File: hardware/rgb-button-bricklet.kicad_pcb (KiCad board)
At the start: 2 copper layers, 25 x 25 mm, 23 parts, among them P1 CON-SENSOR, P2 Boot, SW1 RGB_SWITCH_AD, U1 XMC1XXX24, U2 DRILL, U3 DRILL, U4 DRILL, U5 DRILL

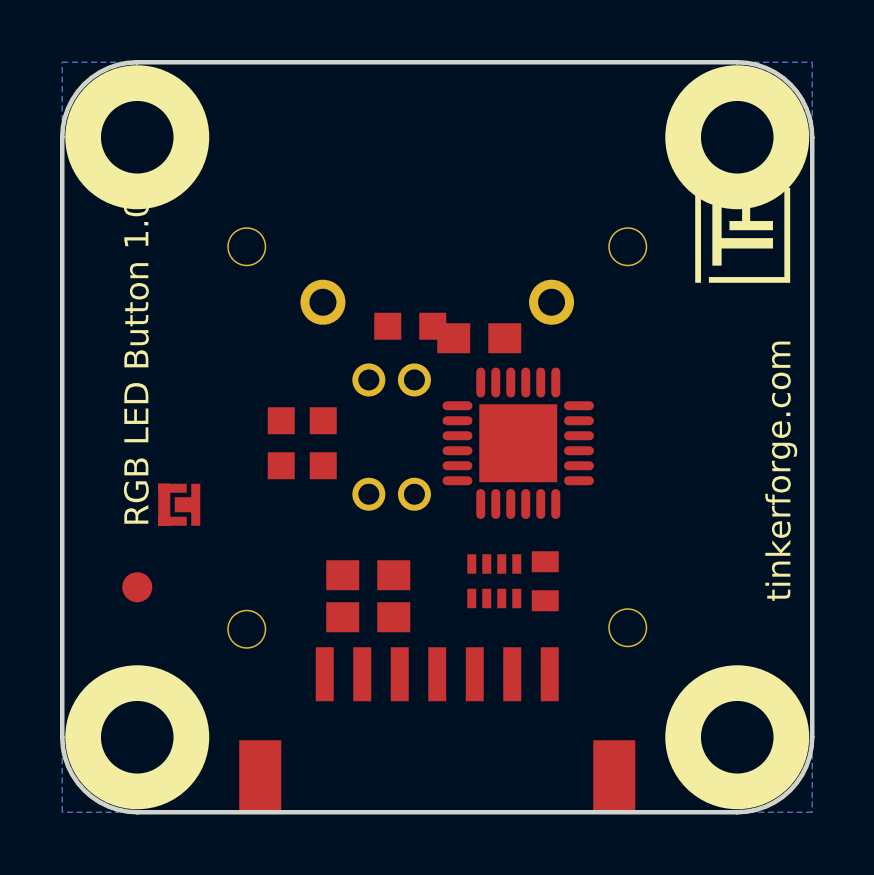
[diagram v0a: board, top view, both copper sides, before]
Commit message: change bricklet to 25x25mm size
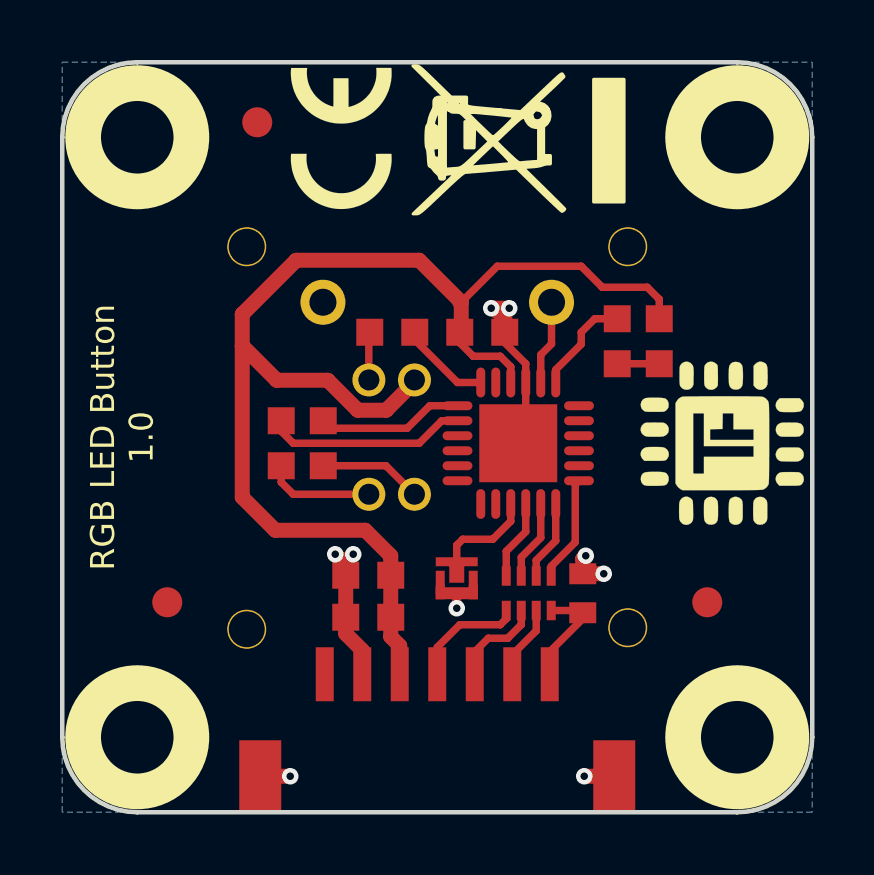
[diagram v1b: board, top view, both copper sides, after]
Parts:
- added D1: blue, kicad-libraries:D0603F, F.Cu at (159.1, 99.2)
- added R4: DNP, R0603F, F.Cu at (146.5, 102.6)
- C1: value 1uF -> TBD; footprint kicad-libraries:C0603E -> C0402E
- C2: value 10uF -> 1uF; footprint kicad-libraries:C0603E -> kicad-libraries:C0603F
- C3: value 100nF -> 10uF; footprint kicad-libraries:C0603E -> kicad-libraries:C0603F
- C4: value TBD -> 100nF; footprint kicad-libraries:C0402E -> kicad-libraries:C0603F
- G*** (x2), VAL: moved to F.Cu
- G***: moved to B.Cu
- R1: value DNP -> 1k
- R2, R3: footprint kicad-libraries:R0603F -> R0603F
- RP1: footprint kicad-libraries:4X0402 -> 4X0402
- SW1: footprint kicad-libraries:RGB_SWITCH_AD -> RGB_SWITCH_AD
- moved Fiducial_Mark 15.5 mm to (160.7, 107.9)
- moved G*** 10.5 mm to (161.2, 102.6), turned to 90 degrees
- moved P2 9.57 mm to (152.3, 107.1), turned to 90 degrees
- moved C1 7.19 mm to (156.6, 107.6), turned to 90 degrees
- moved R1 6.92 mm to (157.7, 99.2), turned to 270 degrees
- moved C4 6.02 mm to (149.4, 108.4), turned to 0 degrees
- moved R2 5.23 mm to (150.2, 98.9), turned to 180 degrees
- moved Fiducial_Mark 4.03 mm to (145.7, 91.9)
- moved G*** 3.78 mm to (159.0, 100.8), turned to 270 degrees
- moved VAL 2.60 mm to (148.5, 92.4), turned to 90 degrees
- moved RP1 1.22 mm to (154.8, 107.6)
- moved Fiducial_Mark 1.12 mm to (142.7, 107.9)
- moved G*** 1.00 mm to (154.4, 92.5), turned to 90 degrees
- moved C3 0.22 mm to (153.2, 98.9)
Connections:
- C1 pad 1: GND -> Net-(C1-Pad1)
- C1 pad 2: VCC -> GND
- C4 pad 1: Net-(C4-Pad1) -> GND
- C4 pad 2: GND -> VCC
- P1 pad 7: Net-(C4-Pad1) -> Net-(C1-Pad1)
- R1 pad 1: P1.2_HO -> Net-(R1-Pad1)
- R1 pad 2: Net-(R1-Pad2) -> Net-(D1-Pad2)
- R2 pad 1: P1.1_HO -> P1.2_HO
- R3 pad 1: P1.0_HO -> P1.1_HO
- RP1 pad 4: Net-(C4-Pad1) -> Net-(C1-Pad1)
- SW1 pad 4: Net-(R1-Pad2) -> Net-(R2-Pad2)
- SW1 pad 5: Net-(R2-Pad2) -> Net-(R3-Pad2)
- SW1 pad 6: Net-(R3-Pad2) -> Net-(R4-Pad2)
- U1 pad 15: PinSwitch -> (no net)
- U1 pad 7: (no net) -> Net-(R1-Pad1)
- U1 pad 8: (no net) -> PinSwitch
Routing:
- net VCC: track 0.00 -> 44.9 mm
- net GND: track 0.00 -> 19.8 mm, vias 0 -> 9
- net P1.0_HO: track 0.00 -> 6.95 mm
- net P1.1_HO: track 0.00 -> 4.89 mm
- net Net-(P1-Pad4): track 0.00 -> 4.57 mm
- net Net-(P2-Pad2): track 0.00 -> 3.66 mm
- net Net-(R4-Pad2): track 0.00 -> 3.64 mm
- net Net-(C1-Pad1): track 0.00 -> 3.59 mm
- net S-MISO: track 0.00 -> 3.56 mm
- net Net-(R3-Pad2): track 0.00 -> 3.43 mm
- net Net-(R1-Pad1): track 0.00 -> 3.41 mm
- net Net-(P1-Pad5): track 0.00 -> 3.15 mm
- net P1.2_HO: track 0.00 -> 3.04 mm
- net PinSwitch: track 0.00 -> 2.82 mm
- net S-MOSI: track 0.00 -> 2.67 mm
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
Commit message: fix text positions
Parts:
- moved G*** 5.22 mm to (160.1, 95.7)
- moved G*** 1.10 mm to (160.7, 103.5)
- moved VAL 0.70 mm to (148.5, 93.1)
- moved G*** 0.62 mm to (154.6, 93.1)
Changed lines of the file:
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@@
     (links 41)
     (no_connects 0)
-    (area 139.124999 89.824999 164.275001 114.975001)
+    (area 138.344999 89.044999 278.84286 159.815)
     (thickness 1.6)
     (drawings 12)
@@
     (35 F.Paste user)
     (36 B.SilkS user)
-    (37 F.SilkS user)
+    (37 F.SilkS user hide)
     (38 B.Mask user)
     (39 F.Mask user)
@@
   )
   (module kicad-libraries:Logo_CoMCU (layer F.Cu)
-    (at 161.2 102.6 90)
+    (at 160.65 103.55 90)
     (fp_text reference G*** (at 0 0 90) (layer F.SilkS) hide
       (effects (font (thickness 0.3)))
@@
   )
   (module kicad-libraries:Logo_31x31 (layer B.Cu)
-    (at 159 100.8 270)
+    (at 160.1 95.7 270)
     (fp_text reference G*** (at 1.34874 -2.97434 270) (layer B.SilkS) hide
       (effects (font (size 0.29972 0.29972) (thickness 0.0762)) (justify mirror))
@@
   )
   (module kicad-libraries:WEEE_7mm (layer F.Cu)
-    (at 154.4 92.5 90)
+    (at 154.55 93.1 90)
     (fp_text reference G*** (at 0 0 90) (layer F.SilkS) hide
       (effects (font (thickness 0.3)))
@@
   )
   (module kicad-libraries:CE_5mm (layer F.Cu)
-    (at 148.5 92.4 90)
+    (at 148.5 93.1 90)
     (fp_text reference VAL (at 0 0 90) (layer F.SilkS) hide
       (effects (font (size 1.143 1.143) (thickness 0.1778)))
@@
     )
   )
-  (gr_text "RGB LED Button\n1.0" (at 141.2 102.4 90) (layer B.SilkS)
+  (gr_text "RGB LED Button\n1.0" (at 141.85 102.4 90) (layer B.SilkS)
     (effects (font (size 0.8 0.8) (thickness 0.15)) (justify mirror))
   )
@@
     (effects (font (size 0.8 0.8) (thickness 0.15)))
   )
-  (gr_text tinkerforge.com (at 163 102.4 90) (layer B.SilkS)
+  (gr_text tinkerforge.com (at 161.65 104.55 90) (layer B.SilkS)
     (effects (font (size 0.8 0.8) (thickness 0.15)) (justify mirror))
   )

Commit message: specify filter circuit
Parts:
- C1: value TBD -> 220pF
- RP1: value TBD -> 82
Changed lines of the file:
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@@
     (links 41)
     (no_connects 0)
-    (area 138.344999 89.044999 278.84286 159.815)
+    (area 139.124999 89.824999 164.275001 114.975001)
     (thickness 1.6)
     (drawings 12)
@@
   (module RGB_SWITCH_AD (layer B.Cu)
     (at 151.7 102.4)
-    (fp_text reference SW1 (at 3.27 6.6) (layer B.Fab)
+    (fp_text reference SW1 (at 6.1 2.9) (layer B.Fab)
       (effects (font (size 0.3 0.3) (thickness 0.075)) (justify mirror))
     )
@@
       (effects (font (size 0.2 0.2) (thickness 0.05)))
     )
-    (fp_text value TBD (at 0 -0.275 90) (layer F.Fab)
+    (fp_text value 220pF (at 0 -0.275 90) (layer F.Fab)
       (effects (font (size 0.2 0.2) (thickness 0.05)))
     )
@@
       (effects (font (size 0.2 0.2) (thickness 0.05)))
     )
-    (fp_text value TBD (at -0.025 -0.45) (layer F.Fab)
+    (fp_text value 82 (at -0.025 -0.45) (layer F.Fab)
       (effects (font (size 0.2 0.2) (thickness 0.05)))
     )

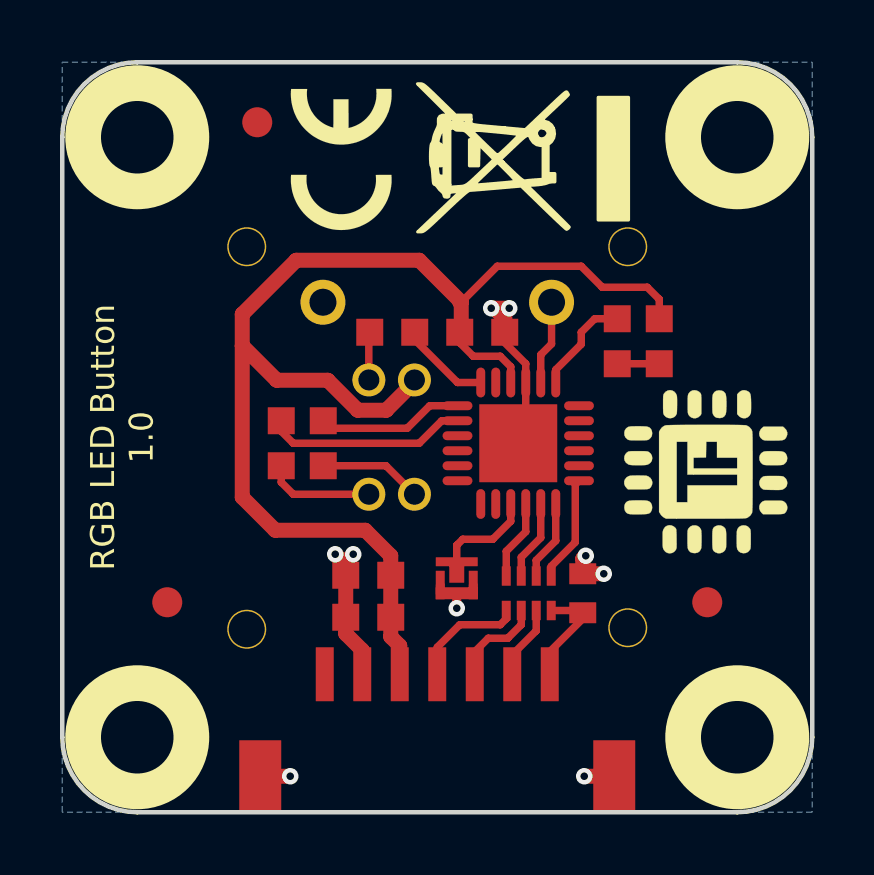
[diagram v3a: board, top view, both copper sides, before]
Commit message: fix rgb button footprint, specify resistors
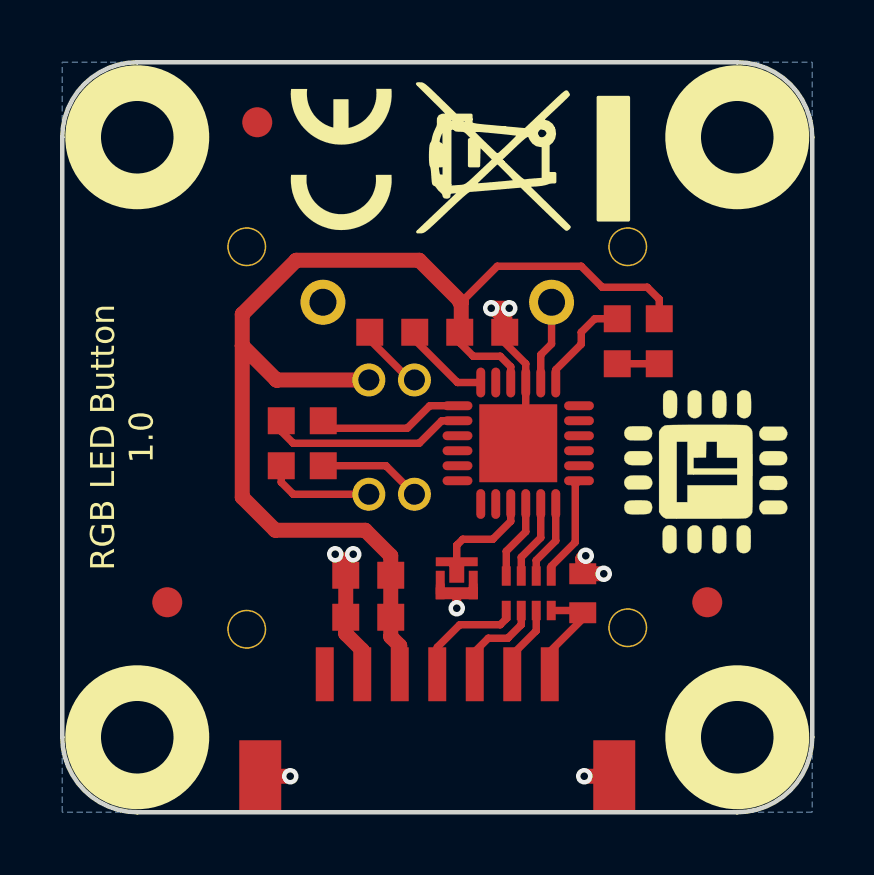
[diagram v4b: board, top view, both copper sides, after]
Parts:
- R2, R4: value DNP -> 15
- R3: value DNP -> 68
- SW1: footprint RGB_SWITCH_AD -> kicad-libraries:RGB_SWITCH_AD
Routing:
- net VCC: track 44.9 -> 42.6 mm
- net Net-(R2-Pad2): track 1.60 -> 2.41 mm
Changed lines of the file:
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@@
     (links 41)
     (no_connects 0)
-    (area 139.124999 89.824999 164.275001 114.975001)
+    (area 138.344999 89.044999 278.84286 159.815)
     (thickness 1.6)
     (drawings 12)
@@
     (add_net VCC)
   )
-  (module RGB_SWITCH_AD (layer B.Cu)
-    (at 151.7 102.4)
-    (fp_text reference SW1 (at 6.1 2.9) (layer B.Fab)
-      (effects (font (size 0.3 0.3) (thickness 0.075)) (justify mirror))
-    )
-    (fp_text value RGB_SWITCH_AD (at 0.2 3) (layer B.Fab)
-      (effects (font (size 0.3 0.3) (thickness 0.075)) (justify mirror))
-    )
-    (fp_line (start -7.5 7.5) (end 7.5 7.5) (layer B.Fab) (width 0.15))
-    (fp_line (start 7.5 7.5) (end 7.5 -7.5) (layer B.Fab) (width 0.15))
-    (fp_line (start 7.5 -7.5) (end -7.5 -7.5) (layer B.Fab) (width 0.15))
-    (fp_line (start -7.5 -7.5) (end -7.5 7.5) (layer B.Fab) (width 0.15))
-    (pad "" np_thru_hole circle (at -6.35 6.4) (size 1.3 1.3) (drill 1.2) (layers *.Cu *.Mask B.SilkS))
-    (pad "" np_thru_hole circle (at 6.35 6.35) (size 1.3 1.3) (drill 1.2) (layers *.Cu *.Mask B.SilkS))
-    (pad "" np_thru_hole circle (at 6.35 -6.35) (size 1.3 1.3) (drill 1.2) (layers *.Cu *.Mask B.SilkS))
-    (pad "" np_thru_hole circle (at -6.35 -6.35) (size 1.3 1.3) (drill 1.2) (layers *.Cu *.Mask B.SilkS))
-    (pad 1 thru_hole circle (at 3.81 -4.5) (size 1.5 1.5) (drill 0.9) (layers *.Cu *.Mask B.SilkS)
-      (net 10 PinSwitch))
-    (pad 2 thru_hole circle (at -3.81 -4.5) (size 1.5 1.5) (drill 0.9) (layers *.Cu *.Mask B.SilkS)
-      (net 1 GND))
-    (pad 6 thru_hole circle (at -2.28 1.9) (size 1.1 1.1) (drill 0.7) (layers *.Cu *.Mask B.SilkS)
-      (net 20 "Net-(R4-Pad2)"))
-    (pad 5 thru_hole circle (at -0.76 1.9) (size 1.1 1.1) (drill 0.7) (layers *.Cu *.Mask B.SilkS)
-      (net 12 "Net-(R3-Pad2)"))
-    (pad 4 thru_hole circle (at -2.28 -1.91) (size 1.1 1.1) (drill 0.7) (layers *.Cu *.Mask B.SilkS)
-      (net 11 "Net-(R2-Pad2)"))
-    (pad 3 thru_hole circle (at -0.76 -1.91) (size 1.1 1.1) (drill 0.7) (layers *.Cu *.Mask B.SilkS)
-      (net 2 VCC))
-  )
   (module kicad-libraries:Logo_CoMCU (layer F.Cu)
     (at 160.65 103.55 90)
@@
       (effects (font (size 0.2 0.2) (thickness 0.05)))
     )
-    (fp_text value DNP (at 0.05 -0.375 180) (layer F.Fab)
+    (fp_text value 15 (at 0.05 -0.375 180) (layer F.Fab)
       (effects (font (size 0.2 0.2) (thickness 0.05)))
     )
@@
       (effects (font (size 0.2 0.2) (thickness 0.05)))
     )
-    (fp_text value DNP (at 0.05 -0.375 270) (layer F.Fab)
+    (fp_text value 68 (at 0.05 -0.375 270) (layer F.Fab)
       (effects (font (size 0.2 0.2) (thickness 0.05)))
     )
@@
       (effects (font (size 0.2 0.2) (thickness 0.05)))
     )
-    (fp_text value DNP (at 0.05 -0.375 270) (layer F.Fab)
+    (fp_text value 15 (at 0.05 -0.375 270) (layer F.Fab)
       (effects (font (size 0.2 0.2) (thickness 0.05)))
     )
@@
     )
   )
+  (module kicad-libraries:RGB_SWITCH_AD (layer B.Cu)
+    (at 151.7 102.4)
+    (fp_text reference SW1 (at 6.1 2.9) (layer B.Fab)
+      (effects (font (size 0.3 0.3) (thickness 0.075)) (justify mirror))
+    )
+    (fp_text value RGB_SWITCH_AD (at 0.2 3) (layer B.Fab)
+      (effects (font (size 0.3 0.3) (thickness 0.075)) (justify mirror))
+    )
+    (fp_line (start -7.5 7.5) (end 7.5 7.5) (layer B.Fab) (width 0.15))
+    (fp_line (start 7.5 7.5) (end 7.5 -7.5) (layer B.Fab) (width 0.15))
+    (fp_line (start 7.5 -7.5) (end -7.5 -7.5) (layer B.Fab) (width 0.15))
+    (fp_line (start -7.5 -7.5) (end -7.5 7.5) (layer B.Fab) (width 0.15))
+    (pad "" np_thru_hole circle (at -6.35 6.4) (size 1.3 1.3) (drill 1.2) (layers *.Cu *.Mask B.SilkS))
+    (pad "" np_thru_hole circle (at 6.35 6.35) (size 1.3 1.3) (drill 1.2) (layers *.Cu *.Mask B.SilkS))
+    (pad "" np_thru_hole circle (at 6.35 -6.35) (size 1.3 1.3) (drill 1.2) (layers *.Cu *.Mask B.SilkS))
+    (pad "" np_thru_hole circle (at -6.35 -6.35) (size 1.3 1.3) (drill 1.2) (layers *.Cu *.Mask B.SilkS))
+    (pad 1 thru_hole circle (at 3.81 -4.5) (size 1.5 1.5) (drill 0.9) (layers *.Cu *.Mask B.SilkS)
+      (net 10 PinSwitch))
+    (pad 2 thru_hole circle (at -3.81 -4.5) (size 1.5 1.5) (drill 0.9) (layers *.Cu *.Mask B.SilkS)
+      (net 1 GND))
+    (pad G2 thru_hole circle (at -2.28 1.9) (size 1.1 1.1) (drill 0.7) (layers *.Cu *.Mask B.SilkS)
+      (net 20 "Net-(R4-Pad2)"))
+    (pad R2 thru_hole circle (at -0.76 1.9) (size 1.1 1.1) (drill 0.7) (layers *.Cu *.Mask B.SilkS)
+      (net 12 "Net-(R3-Pad2)"))
+    (pad C2 thru_hole circle (at -2.28 -1.91) (size 1.1 1.1) (drill 0.7) (layers *.Cu *.Mask B.SilkS)
+      (net 2 VCC))
+    (pad B2 thru_hole circle (at -0.76 -1.91) (size 1.1 1.1) (drill 0.7) (layers *.Cu *.Mask B.SilkS)
+      (net 11 "Net-(R2-Pad2)"))
+  )
   (gr_text "RGB LED Button\n1.0" (at 141.85 102.4 90) (layer B.SilkS)
     (effects (font (size 0.8 0.8) (thickness 0.15)) (justify mirror))
@@
   (segment (start 154.65 100.575) (end 154.65 99.95) (width 0.25) (layer F.Cu) (net 1))
   (segment (start 154.65 99.95) (end 153.95 99.25) (width 0.25) (layer F.Cu) (net 1))
-  (segment (start 150.94 100.49) (end 150.94 100.56) (width 0.5) (layer F.Cu) (net 2))
-  (segment (start 150.94 100.56) (end 150 101.5) (width 0.5) (layer F.Cu) (net 2))
-  (segment (start 150 101.5) (end 149.05 101.5) (width 0.5) (layer F.Cu) (net 2))
-  (segment (start 149.05 101.5) (end 148.05 100.5) (width 0.5) (layer F.Cu) (net 2))
-  (segment (start 148.05 100.5) (end 146.35 100.5) (width 0.5) (layer F.Cu) (net 2))
+  (segment (start 149.42 100.49) (end 146.34 100.49) (width 0.5) (layer F.Cu) (net 2))
   (segment (start 146.35 100.5) (end 145.2 99.35) (width 0.5) (layer F.Cu) (net 2))
+  (segment (start 146.34 100.49) (end 146.35 100.5) (width 0.5) (layer F.Cu) (net 2))
   (segment (start 152.5 97.9) (end 152.5 98.85) (width 0.5) (layer F.Cu) (net 2))
   (segment (start 152.5 98.85) (end 152.45 98.9) (width 0.5) (layer F.Cu) (net 2))
@@
   (segment (start 147 96.5) (end 151.1 96.5) (width 0.5) (layer F.Cu) (net 2))
   (segment (start 145.2 98.3) (end 147 96.5) (width 0.5) (layer F.Cu) (net 2))
-  (segment (start 145.2 104.4) (end 145.2 99.35) (width 0.5) (layer F.Cu) (net 2))
-  (segment (start 145.2 99.35) (end 145.2 98.3) (width 0.5) (layer F.Cu) (net 2))
-  (segment (start 146.3 105.5) (end 145.2 104.4) (width 0.5) (layer F.Cu) (net 2))
-  (segment (start 149.3 105.5) (end 146.3 105.5) (width 0.5) (layer F.Cu) (net 2))
   (segment (start 150.15 106.35) (end 149.3 105.5) (width 0.5) (layer F.Cu) (net 2))
   (segment (start 159.1 98.45) (end 159.1 97.8) (width 0.25) (layer F.Cu) (net 2))
@@
   (segment (start 154.15 100.05) (end 153.8 99.7) (width 0.25) (layer F.Cu) (net 2))
   (segment (start 152.45 99.25) (end 152.45 98.9) (width 0.25) (layer F.Cu) (net 2))
+  (segment (start 145.2 99.35) (end 145.2 98.3) (width 0.5) (layer F.Cu) (net 2))
+  (segment (start 149.3 105.5) (end 146.3 105.5) (width 0.5) (layer F.Cu) (net 2))
+  (segment (start 145.2 104.4) (end 145.2 99.35) (width 0.5) (layer F.Cu) (net 2))
+  (segment (start 146.3 105.5) (end 145.2 104.4) (width 0.5) (layer F.Cu) (net 2))
   (segment (start 155.4993 107.025) (end 155.4993 106.7007) (width 0.25) (layer F.Cu) (net 3))
   (segment (start 155.4993 106.7007) (end 156.3 105.9) (width 0.25) (layer F.Cu) (net 3))
@@
   (segment (start 155.51 99.29) (end 155.51 97.9) (width 0.25) (layer F.Cu) (net 10))
   (segment (start 155.15 99.65) (end 155.51 99.29) (width 0.25) (layer F.Cu) (net 10))
-  (segment (start 149.42 100.49) (end 149.42 98.93) (width 0.25) (layer F.Cu) (net 11))
+  (segment (start 150.94 100.49) (end 150.79 100.49) (width 0.25) (layer F.Cu) (net 11))
+  (segment (start 150.79 100.49) (end 149.45 99.15) (width 0.25) (layer F.Cu) (net 11))
+  (segment (start 149.45 99.15) (end 149.45 98.9) (width 0.25) (layer F.Cu) (net 11))
   (segment (start 149.42 98.93) (end 149.45 98.9) (width 0.25) (layer F.Cu) (net 11))
-  (segment (start 147.9 103.35) (end 149.99 103.35) (width 0.25) (layer F.Cu) (net 12))
+  (segment (start 150.94 100.49) (end 150.94 100.56) (width 0.5) (layer F.Cu) (net 11))
   (segment (start 149.99 103.35) (end 150.94 104.3) (width 0.25) (layer F.Cu) (net 12))
+  (segment (start 147.9 103.35) (end 149.99 103.35) (width 0.25) (layer F.Cu) (net 12))
   (segment (start 152.35 106.95) (end 152.35 106.55) (width 0.2) (layer F.Cu) (net 13))
   (segment (start 154.15 104.625) (end 154.15 105.2) (width 0.25) (layer F.Cu) (net 13))
